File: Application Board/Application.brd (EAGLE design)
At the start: 52.8 x 68.6 mm, 54 parts, among them Q1 DMP2012SN-7, T1 FDN340P, T2 AP1117_LIN_REG, U1 LM3409HV'LM3409HV'

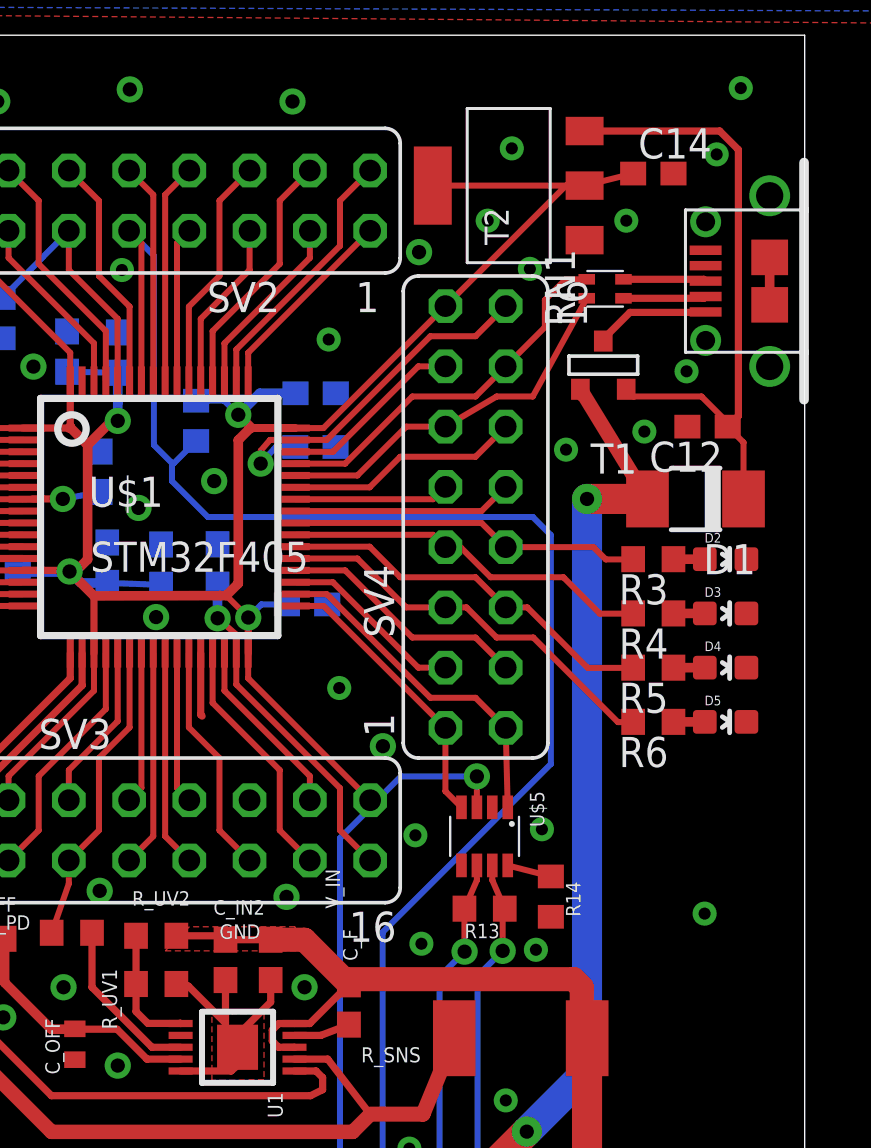
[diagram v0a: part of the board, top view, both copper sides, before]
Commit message: Fixed All The DRC Errors Except The Dimension Errors
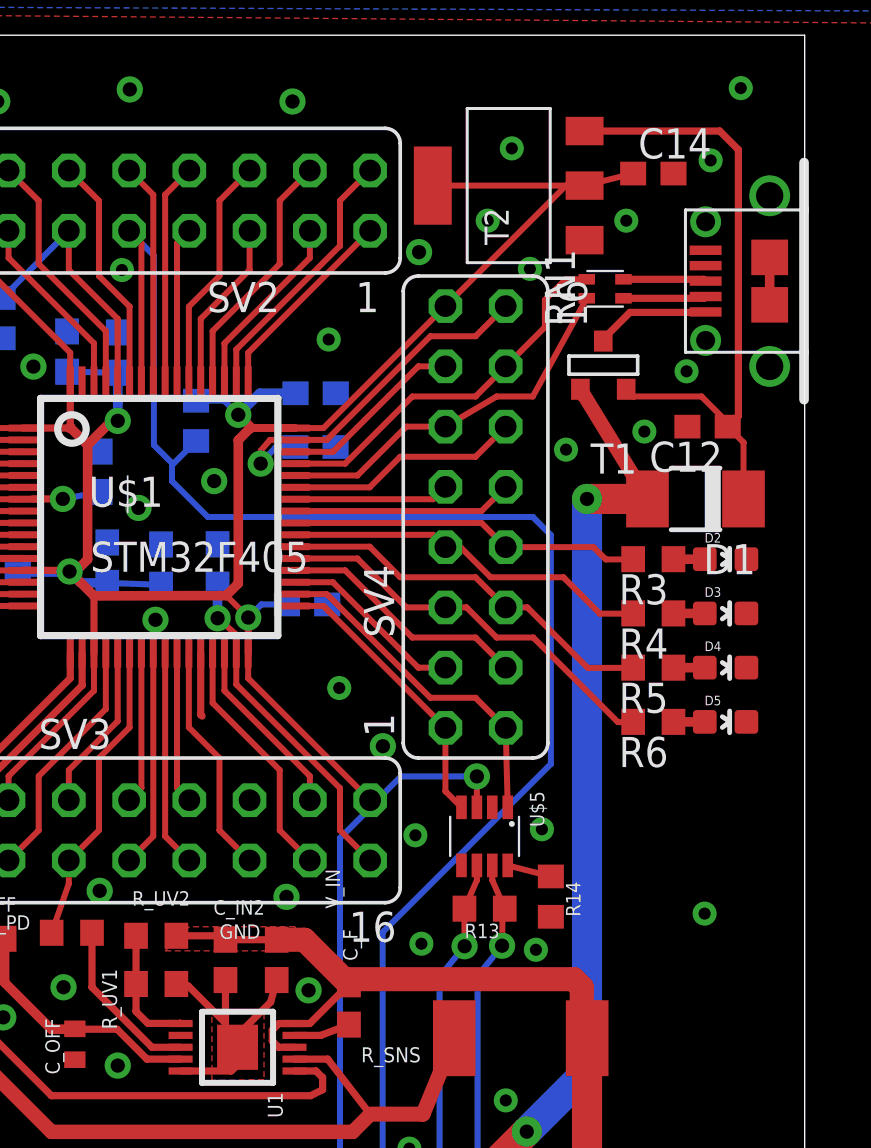
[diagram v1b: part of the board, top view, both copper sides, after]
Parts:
- moved C_IN1 0.25 mm to (27.3, 29.6)
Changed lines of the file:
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@@
 <?xml version="1.0" encoding="utf-8"?>
 <!DOCTYPE eagle SYSTEM "eagle.dtd">
-<eagle version="7.5.0">
+<eagle version="7.4.0">
 <drawing>
 <settings>
@@
 <attribute name="SPICEPREFIX" value="C" x="30.32251875" y="27.721559375" size="1.778" layer="27" rot="R270" display="off"/>
 <attribute name="NAME" x="30.06851875" y="30.896559375" size="0.6096" layer="25" rot="R270"/>
-<attribute name="VALUE" x="28.41751875" y="28.356559375" size="0.6096" layer="27" rot="R270"/>
-</element>
-<element name="C_IN1" library="eagle-ltspice" package="C0603" value="2.2E-6" x="27.02051875" y="29.601159375" smashed="yes" rot="R270">
-<attribute name="SPICEMODEL" value="NONE" x="27.02051875" y="29.601159375" size="1.778" layer="27" rot="R270" display="off"/>
-<attribute name="SPICEPREFIX" value="C" x="27.02051875" y="29.601159375" size="1.778" layer="27" rot="R270" display="off"/>
-<attribute name="VALUE" x="25.11551875" y="30.236159375" size="0.6096" layer="27" rot="R270"/>
+<attribute name="VALUE" x="29.17951875" y="28.864559375" size="0.6096" layer="27" rot="R270"/>
+</element>
+<element name="C_IN1" library="eagle-ltspice" package="C0603" value="2.2E-6" x="27.27451875" y="29.601159375" smashed="yes" rot="R270">
+<attribute name="SPICEMODEL" value="NONE" x="27.27451875" y="29.601159375" size="1.778" layer="27" rot="R270" display="off"/>
+<attribute name="SPICEPREFIX" value="C" x="27.27451875" y="29.601159375" size="1.778" layer="27" rot="R270" display="off"/>
+<attribute name="VALUE" x="25.36951875" y="30.236159375" size="0.6096" layer="27" rot="R270"/>
 </element>
 <element name="C_IN2" library="eagle-ltspice" package="C0603" value="2.2E-6" x="25.11551875" y="29.601159375" smashed="yes" rot="R270">
@@
 <wire x1="25.11551875" y1="28.751159375" x2="25.11551875" y2="26.934159375" width="0.3048" layer="1"/>
 <wire x1="25.11551875" y1="26.934159375" x2="25.62351875" y2="26.426159375" width="0" layer="19" extent="1-16"/>
-<wire x1="27.02051875" y1="28.751159375" x2="27.02051875" y2="27.823159375" width="0.3048" layer="1"/>
+<wire x1="27.27451875" y1="28.751159375" x2="27.02051875" y2="27.823159375" width="0.3048" layer="1"/>
 <wire x1="27.02051875" y1="27.823159375" x2="25.62351875" y2="26.426159375" width="0.3048" layer="1"/>
 <contactref element="SV3" pad="11"/>
@@
 <via x="44.550078125" y="54.411878125" extent="1-16" drill="0.508"/>
 <via x="42.772078125" y="51.871878125" extent="1-16" drill="0.508"/>
-<via x="45.820078125" y="63.555878125" extent="1-16" drill="0.508"/>
+<via x="45.566078125" y="63.301878125" extent="1-16" drill="0.508"/>
 <via x="37.184078125" y="63.809878125" extent="1-16" drill="0.508"/>
 <via x="39.470078125" y="51.109878125" extent="1-16" drill="0.508"/>
@@
 <vertex x="25.908" y="1.524"/>
 </polygon>
-<via x="22.189440625" y="44.051221875" extent="1-16" drill="0.6"/>
+<via x="22.164040625" y="43.936921875" extent="1-16" drill="0.6"/>
 <via x="33.274" y="59.436" extent="1-16" drill="0.6"/>
 <wire x1="36.168078125" y1="60.761878125" x2="33.274" y2="59.436" width="0" layer="19" extent="1-1"/>
@@
 <contactref element="U$2" pad="B33"/>
 <wire x1="35.18751875" y1="31.760159375" x2="35.18751875" y2="29.949140625" width="0.254" layer="1"/>
-<wire x1="35.18751875" y1="29.949140625" x2="35.1942375" y2="29.949140625" width="0.254" layer="1"/>
-<via x="35.1942375" y="29.949140625" extent="1-16" drill="0.6"/>
-<wire x1="35.1942375" y1="29.949140625" x2="34.14151875" y2="28.896421875" width="0.254" layer="16"/>
+<wire x1="35.18751875" y1="29.949140625" x2="35.1942375" y2="30.177740625" width="0.254" layer="1"/>
+<via x="35.1942375" y="30.177740625" extent="1-16" drill="0.6"/>
+<wire x1="35.1942375" y1="30.177740625" x2="34.14151875" y2="28.896421875" width="0.254" layer="16"/>
 <wire x1="34.14151875" y1="28.896421875" x2="34.14151875" y2="2.410159375" width="0.254" layer="16"/>
 </signal>
@@
 <contactref element="U$2" pad="B35"/>
 <wire x1="36.88751875" y1="31.760159375" x2="36.79951875" y2="31.672159375" width="0.254" layer="1"/>
-<wire x1="36.79951875" y1="31.672159375" x2="36.79951875" y2="29.982159375" width="0.254" layer="1"/>
-<via x="36.79951875" y="29.982159375" extent="1-16" drill="0.6"/>
-<wire x1="36.79951875" y1="29.982159375" x2="35.74151875" y2="28.924159375" width="0.254" layer="16"/>
+<wire x1="36.79951875" y1="31.672159375" x2="36.77411875" y2="30.198059375" width="0.254" layer="1"/>
+<via x="36.77411875" y="30.198059375" extent="1-16" drill="0.6"/>
+<wire x1="36.77411875" y1="30.198059375" x2="35.74151875" y2="28.924159375" width="0.254" layer="16"/>
 <wire x1="35.74151875" y1="28.924159375" x2="35.74151875" y2="2.410159375" width="0.254" layer="16"/>
 </signal>
@@
 <contactref element="U1" pad="10"/>
 <contactref element="U1" pad="8"/>
-<wire x1="27.02051875" y1="30.451159375" x2="27.02051875" y2="30.490159375" width="0.4064" layer="1"/>
+<wire x1="27.27451875" y1="30.451159375" x2="27.02051875" y2="30.490159375" width="0.4064" layer="1"/>
 <wire x1="30.32251875" y1="28.571559375" x2="30.39871875" y2="28.559759375" width="0.635" layer="1"/>
 <wire x1="30.39871875" y1="28.559759375" x2="30.34791875" y2="28.788359375" width="0.635" layer="1"/>
 <wire x1="23.04451875" y1="30.617159375" x2="25.20351875" y2="30.617159375" width="0.3048" layer="1"/>
 <wire x1="25.20351875" y1="30.617159375" x2="25.11551875" y2="30.451159375" width="0.3048" layer="1"/>
-<wire x1="25.11551875" y1="30.451159375" x2="27.02051875" y2="30.451159375" width="0.3048" layer="1"/>
-<wire x1="27.02051875" y1="30.451159375" x2="28.44291875" y2="30.451159375" width="1.016" layer="1"/>
+<wire x1="25.11551875" y1="30.451159375" x2="27.27451875" y2="30.451159375" width="0.3048" layer="1"/>
+<wire x1="27.27451875" y1="30.451159375" x2="28.44291875" y2="30.451159375" width="1.016" layer="1"/>
 <wire x1="28.44291875" y1="30.451159375" x2="30.32251875" y2="28.571559375" width="1.016" layer="1"/>
 <wire x1="28.02381875" y1="26.91891875" x2="28.669878125" y2="26.91891875" width="0.3048" layer="1"/>
@@
 </signal>
 <signal name="N$33">
-<via x="28.448" y="28.448" extent="1-16" drill="0.6"/>
+<via x="28.618178125" y="28.3184625" extent="1-16" drill="0.6"/>
 </signal>
 <signal name="N$23">

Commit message: Board Layout Finished！
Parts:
- C_F: value 1.0E-6 -> 1.0uF
- C_IN1, C_IN2: value 2.2E-6 -> 2.2uF
- C_OFF: value 470E-12 -> 470pF
- L1: value 15E-6 -> 15u
- S1: value SWITCH -> BOOT
- S2: value SWITCH -> RESET
- moved RN1 0.76 mm to (41.9, 57.9)
- moved S2 0.51 mm to (3.53, 44.5)
- moved ASV 0.25 mm to (3.27, 55.9)
- moved R_PD 0.25 mm to (18.6, 30.5)
- moved R_SNS 0.25 mm to (37.6, 26.0)
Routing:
- net GND: track 29.6 -> 38.9 mm, vias 44 -> 53
- net OSCIN: track 20.4 -> 17.9 mm
- net +3V3: track 187.3 -> 185.2 mm
- net NRST: track 21.8 -> 20.0 mm
- net N$24: track 3.49 -> 2.73 mm
- net N$1: track 3.49 -> 2.73 mm
- net USBD+: track 16.2 -> 16.9 mm
- net N$58: track 27.0 -> 27.7 mm
- added copper zone on layer 1, net N$22
- added copper zone on layer 16, net N$26
- added copper zone on layer 16, net N$27
- added copper zone on layer 1, net N$28
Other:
- board text added: "+12V"
- board text added: "+5V"
- board text added: "CAM_LEDV"
- board text added: "C_IN1"
- board text removed: "GND"
- board text removed: "V_IN"
